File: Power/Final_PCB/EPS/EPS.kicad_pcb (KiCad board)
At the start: 2 copper layers, 85 x 85 mm, 36 parts, among them J1 Left_Header, J2 Right_Header, U1 INA226, U2 MT3608-28, U3 LM2596S-5, U4 LM2596S-3.3

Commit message: Silkscreen Addition
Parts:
- added .: ., LOGO, B.Cu at (93.0, 91.0)
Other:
- board text added: "HYPERIONyX 2026 Designed by Rohaan.K"

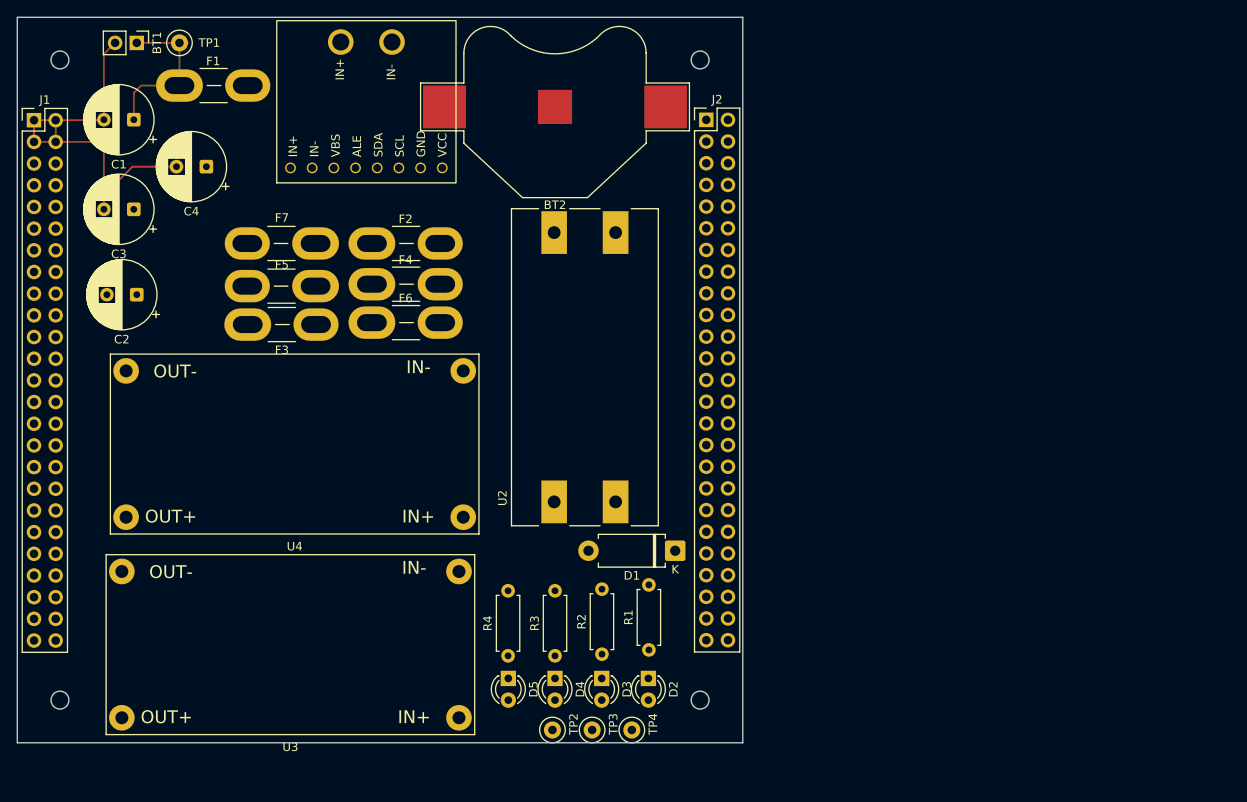
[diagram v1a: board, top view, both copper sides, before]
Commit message: Finalised EPS tracks/connections
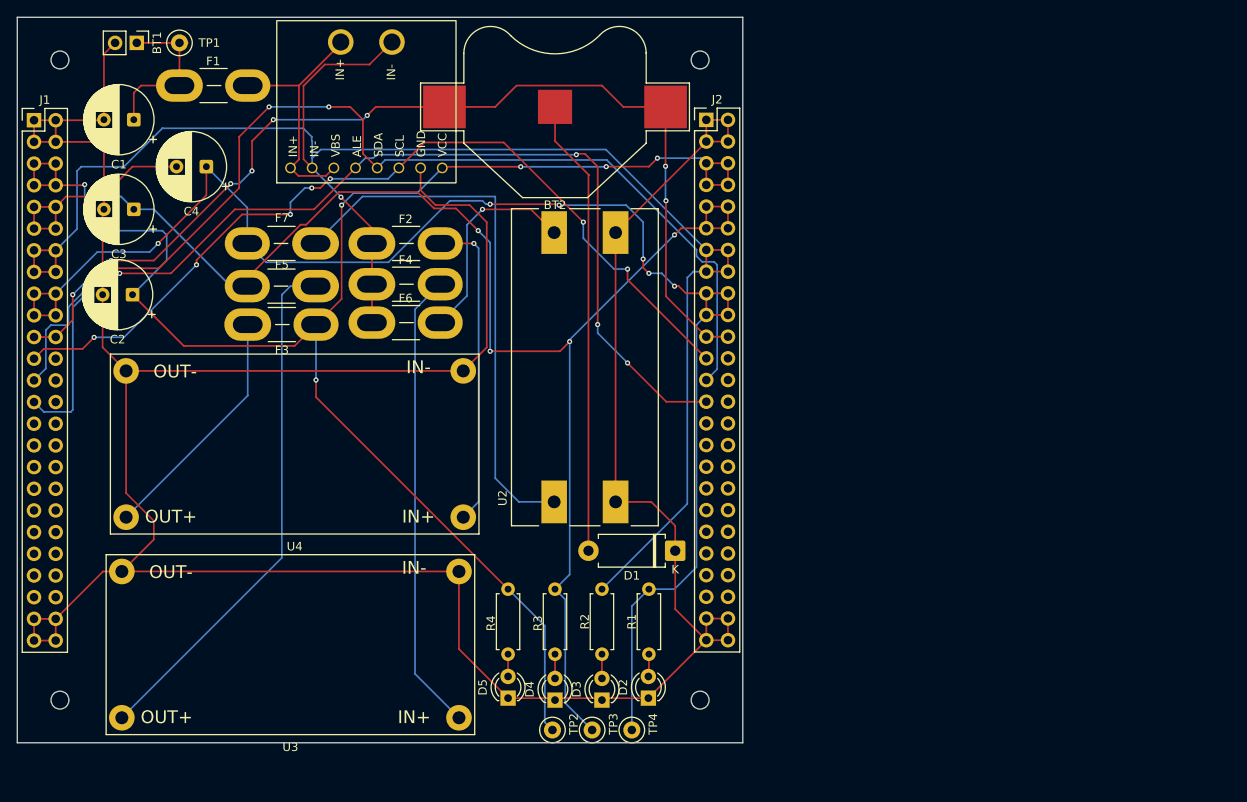
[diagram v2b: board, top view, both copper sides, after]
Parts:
- moved R3 7.81 mm to (113.0, 111.0), turned to -90 degrees
- moved R4 7.81 mm to (107.5, 111.0), turned to -90 degrees
- moved R2 7.62 mm to (118.5, 111.0), turned to -90 degrees
- moved R1 7.12 mm to (124.0, 111.0), turned to -90 degrees
- moved D3 2.54 mm to (118.5, 124.0), turned to 90 degrees
- moved D4 2.54 mm to (113.0, 124.0), turned to 90 degrees
- moved D5 2.31 mm to (107.5, 123.8), turned to 90 degrees
- moved D2 2.31 mm to (123.9, 123.8), turned to 90 degrees
- moved C2 0.50 mm to (63.5, 76.5)
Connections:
- J1 pad 24: SDA -> XB_RESET
- J1 pad 25: INA_ALERT -> SDA
- J1 pad 26: unconnected-(J1-Pin_26-Pad26) -> BNO_INT
- J1 pad 27: unconnected-(J1-Pin_27-Pad27) -> INA_ALERT
- J1 pad 28: unconnected-(J1-Pin_28-Pad28) -> L298N_2_ENA
- J1 pad 29: unconnected-(J1-Pin_29-Pad29) -> L298N_2_IN4
- J1 pad 30: unconnected-(J1-Pin_30-Pad30) -> L298N_2_IN3
- J1 pad 31: unconnected-(J1-Pin_31-Pad31) -> L298N_2_IN2
- J1 pad 32: unconnected-(J1-Pin_32-Pad32) -> L298N_2_IN1
- J1 pad 33: unconnected-(J1-Pin_33-Pad33) -> L298N_1_ENB
- J1 pad 34: unconnected-(J1-Pin_34-Pad34) -> L298N_1_ENA
- J1 pad 35: unconnected-(J1-Pin_35-Pad35) -> L298N_1_IN4
- J1 pad 36: unconnected-(J1-Pin_36-Pad36) -> L298N_1_IN3
- J1 pad 37: unconnected-(J1-Pin_37-Pad37) -> L298N_1_IN2
- J1 pad 38: unconnected-(J1-Pin_38-Pad38) -> L298N_1_IN1
- J1 pad 39: unconnected-(J1-Pin_39-Pad39) -> BPW34_OUT
- J1 pad 40: unconnected-(J1-Pin_40-Pad40) -> GNSS_PPS
- J1 pad 41: unconnected-(J1-Pin_41-Pad41) -> GNSS_FIX
- J1 pad 42: unconnected-(J1-Pin_42-Pad42) -> GNSS_EN
- J1 pad 43: unconnected-(J1-Pin_43-Pad43) -> RX2
- J1 pad 44: unconnected-(J1-Pin_44-Pad44) -> RX1
- J1 pad 45: GND -> TX2
- J1 pad 46: GND -> TX1
- J2 pad 24: SDA -> XB_RESET
- J2 pad 25: INA_ALERT -> SDA
- J2 pad 26: unconnected-(J2-Pin_26-Pad26) -> BNO_INT
- J2 pad 27: unconnected-(J2-Pin_27-Pad27) -> INA_ALERT
- J2 pad 28: unconnected-(J2-Pin_28-Pad28) -> L298N_2_ENA
- J2 pad 29: unconnected-(J2-Pin_29-Pad29) -> L298N_2_IN4
- J2 pad 30: unconnected-(J2-Pin_30-Pad30) -> L298N_2_IN3
- J2 pad 31: unconnected-(J2-Pin_31-Pad31) -> L298N_2_IN2
- J2 pad 32: unconnected-(J2-Pin_32-Pad32) -> L298N_2_IN1
- J2 pad 33: unconnected-(J2-Pin_33-Pad33) -> L298N_1_ENB
- J2 pad 34: unconnected-(J2-Pin_34-Pad34) -> L298N_1_ENA
- J2 pad 35: unconnected-(J2-Pin_35-Pad35) -> L298N_1_IN4
- J2 pad 36: unconnected-(J2-Pin_36-Pad36) -> L298N_1_IN3
- J2 pad 37: unconnected-(J2-Pin_37-Pad37) -> L298N_1_IN2
- J2 pad 38: unconnected-(J2-Pin_38-Pad38) -> L298N_1_IN1
- J2 pad 39: unconnected-(J2-Pin_39-Pad39) -> BPW34_OUT
- J2 pad 40: unconnected-(J2-Pin_40-Pad40) -> GNSS_PPS
- J2 pad 41: unconnected-(J2-Pin_41-Pad41) -> GNSS_FIX
- J2 pad 42: unconnected-(J2-Pin_42-Pad42) -> GNSS_EN
- J2 pad 43: unconnected-(J2-Pin_43-Pad43) -> RX2
- J2 pad 44: unconnected-(J2-Pin_44-Pad44) -> RX1
- J2 pad 45: GND -> TX2
- J2 pad 46: GND -> TX1
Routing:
- net GND: track 49.9 -> 359.3 mm
- net 14.8V: track 0.00 -> 202.6 mm, vias 0 -> 1
- net 3V3: track 0.00 -> 191.0 mm, vias 0 -> 10
- net 28V: track 0.00 -> 176.4 mm, vias 0 -> 6
- net 5V: track 0.00 -> 175.8 mm, vias 0 -> 6
- net SDA: track 0.00 -> 125.9 mm, vias 0 -> 3
- net INA_ALERT: track 0.00 -> 122.6 mm, vias 0 -> 4
- net VBAT: track 0.00 -> 122.5 mm, vias 0 -> 9
- net SCL: track 0.00 -> 102.9 mm, vias 0 -> 7
- net L298N_1_IN3: track 0.00 -> 82.4 mm
- net GNSS_PPS: track 0.00 -> 82.2 mm
- net L298N_1_IN2: track 0.00 -> 81.2 mm
- net RX1: track 0.00 -> 81.0 mm
- net L298N_1_IN1: track 0.00 -> 80.9 mm
- net GNSS_FIX: track 0.00 -> 80.3 mm
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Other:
- copper layers 2 -> 4

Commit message: Transitioned to ADCS-free version for worst case manufacturing scenario
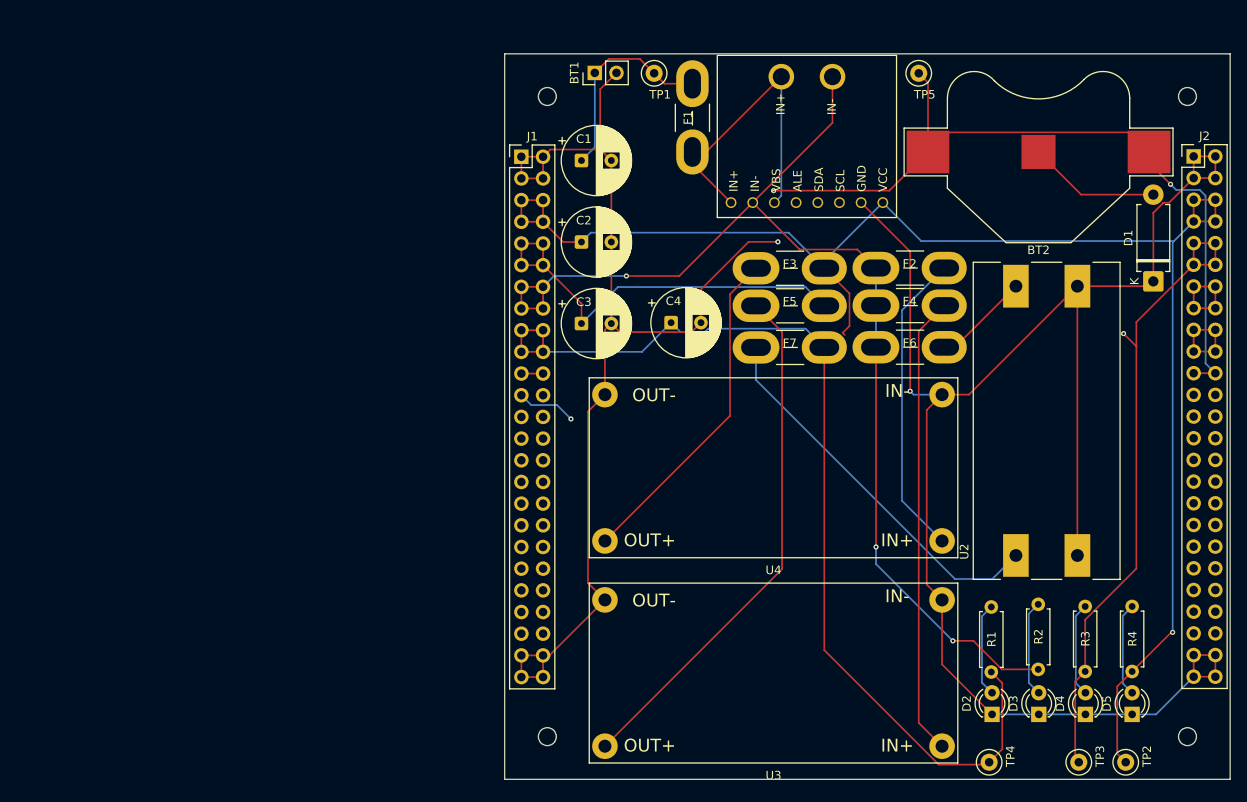
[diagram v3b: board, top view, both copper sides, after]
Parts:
- removed the REF** at (130.0, 124.0)
- removed the REF** at (55.0, 124.0)
- removed the REF** at (130.0, 49.0)
- removed the REF** at (55.0, 49.0)
- added REF**: MountingHole_2.1mm, MountingHole:MountingHole_2.1mm, F.Cu at (112.1, 128.3)
- added REF**: MountingHole_2.1mm, MountingHole:MountingHole_2.1mm, F.Cu at (187.1, 128.3)
- added REF**: MountingHole_2.1mm, MountingHole:MountingHole_2.1mm, F.Cu at (187.1, 53.3)
- added REF**: MountingHole_2.1mm, MountingHole:MountingHole_2.1mm, F.Cu at (112.1, 53.3)
- added TP5: TestPoint, TestPoint:TestPoint_Loop_D2.50mm_Drill1.0mm, F.Cu at (155.6, 50.6)
- moved R4 73.7 mm to (180.6, 120.7), turned to 90 degrees
- moved D5 73.1 mm to (180.6, 125.7)
- moved TP2 67.3 mm to (179.9, 131.3)
- moved D1 64.3 mm to (183.1, 74.9), turned to 90 degrees
- moved R3 62.9 mm to (175.1, 120.7), turned to 90 degrees
- moved D4 62.2 mm to (175.1, 125.7)
- moved F1 60.1 mm to (129.1, 51.8), turned to -90 degrees
- moved F3 59.9 mm to (136.6, 73.4)
- moved F2 59.1 mm to (150.6, 73.4)
- moved F6 59.1 mm to (150.6, 82.7)
- moved F4 59.1 mm to (150.6, 77.8)
- moved . 58.9 mm to (151.1, 100.6)
- moved C4 57.4 mm to (126.6, 79.8), turned to 0 degrees
- moved J1 57.3 mm to (109.1, 60.3)
- moved J2 57.3 mm to (187.8, 60.3)
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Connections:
- J1 pad 28: L298N_2_ENA -> unconnected-(J1-Pin_28-Pad28)
- J1 pad 29: L298N_2_IN4 -> unconnected-(J1-Pin_29-Pad29)
- J1 pad 30: L298N_2_IN3 -> unconnected-(J1-Pin_30-Pad30)
- J1 pad 31: L298N_2_IN2 -> unconnected-(J1-Pin_31-Pad31)
- J1 pad 32: L298N_2_IN1 -> unconnected-(J1-Pin_32-Pad32)
- J1 pad 33: L298N_1_ENB -> unconnected-(J1-Pin_33-Pad33)
- J1 pad 34: L298N_1_ENA -> unconnected-(J1-Pin_34-Pad34)
- J1 pad 35: L298N_1_IN4 -> unconnected-(J1-Pin_35-Pad35)
- J1 pad 36: L298N_1_IN3 -> unconnected-(J1-Pin_36-Pad36)
- J1 pad 37: L298N_1_IN2 -> unconnected-(J1-Pin_37-Pad37)
- J1 pad 38: L298N_1_IN1 -> unconnected-(J1-Pin_38-Pad38)
- J2 pad 28: L298N_2_ENA -> unconnected-(J2-Pin_28-Pad28)
- J2 pad 29: L298N_2_IN4 -> unconnected-(J2-Pin_29-Pad29)
- J2 pad 30: L298N_2_IN3 -> unconnected-(J2-Pin_30-Pad30)
- J2 pad 31: L298N_2_IN2 -> unconnected-(J2-Pin_31-Pad31)
- J2 pad 32: L298N_2_IN1 -> unconnected-(J2-Pin_32-Pad32)
- J2 pad 33: L298N_1_ENB -> unconnected-(J2-Pin_33-Pad33)
- J2 pad 34: L298N_1_ENA -> unconnected-(J2-Pin_34-Pad34)
- J2 pad 35: L298N_1_IN4 -> unconnected-(J2-Pin_35-Pad35)
- J2 pad 36: L298N_1_IN3 -> unconnected-(J2-Pin_36-Pad36)
- J2 pad 37: L298N_1_IN2 -> unconnected-(J2-Pin_37-Pad37)
- J2 pad 38: L298N_1_IN1 -> unconnected-(J2-Pin_38-Pad38)
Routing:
- net L298N_1_IN3: track 82.4 -> 0.00 mm
- net L298N_1_IN2: track 81.2 -> 0.00 mm
- net L298N_1_IN1: track 80.9 -> 0.00 mm
- net L298N_1_IN4: track 79.8 -> 0.00 mm
- net L298N_2_IN2: track 79.7 -> 0.00 mm
- net L298N_2_IN4: track 79.7 -> 0.00 mm
- net L298N_2_IN3: track 79.7 -> 0.00 mm
- net L298N_1_ENB: track 79.7 -> 0.00 mm
- net L298N_1_ENA: track 79.7 -> 0.00 mm
- net L298N_2_IN1: track 79.7 -> 0.00 mm
- net L298N_2_ENA: track 79.7 -> 0.00 mm
- net Net-(BT2--): track 53.7 -> 15.5 mm
- net SCL: track 102.9 -> 127.7 mm, vias 7 -> 1
- net 14.8V: track 202.6 -> 182.9 mm, vias 1 -> 4
- net Net-(U2-VOUT+): track 64.4 -> 45.1 mm
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
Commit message: Finalised Sensors PCB
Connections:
- J1 pad 28: unconnected-(J1-Pin_28-Pad28) -> MICROFC
- J1 pad 29: unconnected-(J1-Pin_29-Pad29) -> S1223
- J1 pad 30: unconnected-(J1-Pin_30-Pad30) -> BNO_RST
- J2 pad 28: unconnected-(J2-Pin_28-Pad28) -> MICROFC
- J2 pad 29: unconnected-(J2-Pin_29-Pad29) -> S1223
- J2 pad 30: unconnected-(J2-Pin_30-Pad30) -> BNO_RST
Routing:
- net MICROFC: track 0.00 -> 81.0 mm, vias 0 -> 3
- net BNO_RST: track 0.00 -> 79.9 mm
- net S1223: track 0.00 -> 79.7 mm, vias 0 -> 1
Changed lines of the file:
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@@
 			(layers "*.Cu" "*.Mask")
 			(remove_unused_layers no)
-			(net "unconnected-(J1-Pin_28-Pad28)")
+			(net "MICROFC")
 			(pinfunction "Pin_28_28")
-			(pintype "passive+no_connect")
+			(pintype "passive")
 		)
 		(pad "29" thru_hole circle
@@
 			(layers "*.Cu" "*.Mask")
 			(remove_unused_layers no)
-			(net "unconnected-(J1-Pin_29-Pad29)")
+			(net "S1223")
 			(pinfunction "Pin_29_29")
-			(pintype "passive+no_connect")
+			(pintype "passive")
 		)
 		(pad "30" thru_hole circle
@@
 			(layers "*.Cu" "*.Mask")
 			(remove_unused_layers no)
-			(net "unconnected-(J1-Pin_30-Pad30)")
+			(net "BNO_RST")
 			(pinfunction "Pin_30_30")
-			(pintype "passive+no_connect")
+			(pintype "passive")
 		)
 		(pad "31" thru_hole circle
@@
 			(layers "*.Cu" "*.Mask")
 			(remove_unused_layers no)
-			(net "unconnected-(J2-Pin_28-Pad28)")
+			(net "MICROFC")
 			(pinfunction "Pin_28_28")
-			(pintype "passive+no_connect")
+			(pintype "passive")
 		)
 		(pad "29" thru_hole circle
@@
 			(layers "*.Cu" "*.Mask")
 			(remove_unused_layers no)
-			(net "unconnected-(J2-Pin_29-Pad29)")
+			(net "S1223")
 			(pinfunction "Pin_29_29")
-			(pintype "passive+no_connect")
+			(pintype "passive")
 		)
 		(pad "30" thru_hole circle
@@
 			(layers "*.Cu" "*.Mask")
 			(remove_unused_layers no)
-			(net "unconnected-(J2-Pin_30-Pad30)")
+			(net "BNO_RST")
 			(pinfunction "Pin_30_30")
-			(pintype "passive+no_connect")
+			(pintype "passive")
 		)
 		(pad "31" thru_hole circle
@@
 		(net "Net-(D2-A)")
 	)
+	(segment
+		(start 182.5 95.5)
+		(end 183.53 94.47)
+		(width 0.2)
+		(layer "F.Cu")
+		(net "MICROFC")
+	)
+	(segment
+		(start 113.745 95.505)
+		(end 111.6 93.36)
+		(width 0.2)
+		(layer "F.Cu")
+		(net "MICROFC")
+	)
+	(segment
+		(start 181.75 96)
+		(end 182.25 95.5)
+		(width 0.2)
+		(layer "F.Cu")
+		(net "MICROFC")
+	)
+	(segment
+		(start 183.53 94.47)
+		(end 189.215 94.47)
+		(width 0.2)
+		(layer "F.Cu")
+		(net "MICROFC")
+	)
+	(segment
+		(start 189.215 94.47)
+		(end 190.365 93.32)
+		(width 0.2)
+		(layer "F.Cu")
+		(net "MICROFC")
+	)
+	(segment
+		(start 182.25 95.5)
+		(end 182.5 95.5)
+		(width 0.2)
+		(layer "F.Cu")
+		(net "MICROFC")
+	)
+	(via
+		(at 181.75 96)
+		(size 0.6)
+		(drill 0.3)
+		(layers "F.Cu" "B.Cu")
+		(net "MICROFC")
+	)
+	(via
+		(at 154.5 96)
+		(size 0.6)
+		(drill 0.3)
+		(layers "F.Cu" "B.Cu")
+		(net "MICROFC")
+	)
+	(via
+		(at 113.745 95.505)
+		(size 0.6)
+		(drill 0.3)
+		(layers "F.Cu" "B.Cu")
+		(net "MICROFC")
+	)
+	(segment
+		(start 181.75 96)
+		(end 154.5 96)
+		(width 0.2)
+		(layer "B.Cu")
+		(net "MICROFC")
+	)
+	(segment
+		(start 114.255 95.505)
+		(end 114.75 96)
+		(width 0.2)
+		(layer "In2.Cu")
+		(net "MICROFC")
+	)
+	(segment
+		(start 114.75 96)
+		(end 154.5 96)
+		(width 0.2)
+		(layer "In2.Cu")
+		(net "MICROFC")
+	)
+	(segment
+		(start 113.745 95.505)
+		(end 114.255 95.505)
+		(width 0.2)
+		(layer "In2.Cu")
+		(net "MICROFC")
+	)
+	(via
+		(at 187.825 95.86)
+		(size 0.6)
+		(drill 0.3)
+		(layers "F.Cu" "B.Cu")
+		(net "S1223")
+	)
+	(segment
+		(start 109.06 95.9)
+		(end 110.21 97.05)
+		(width 0.2)
+		(layer "In2.Cu")
+		(net "S1223")
+	)
+	(segment
+		(start 186.635 97.05)
+		(end 187.825 95.86)
+		(width 0.2)
+		(layer "In2.Cu")
+		(net "S1223")
+	)
+	(segment
+		(start 110.21 97.05)
+		(end 186.635 97.05)
+		(width 0.2)
+		(layer "In2.Cu")
+		(net "S1223")
+	)
+	(segment
+		(start 112.95 97.25)
+		(end 111.6 95.9)
+		(width 0.2)
+		(layer "In1.Cu")
+		(net "BNO_RST")
+	)
+	(segment
+		(start 188.975 97.25)
+		(end 112.95 97.25)
+		(width 0.2)
+		(layer "In1.Cu")
+		(net "BNO_RST")
+	)
+	(segment
+		(start 190.365 95.86)
+		(end 188.975 97.25)
+		(width 0.2)
+		(layer "In1.Cu")
+		(net "BNO_RST")
+	)
 	(embedded_fonts no)
